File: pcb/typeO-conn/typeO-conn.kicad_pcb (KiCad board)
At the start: 2 copper layers, 24 x 19.6 mm, 9 parts, among them J1 USB_C_Receptacle_USB2.0, J2 Conn_01x05_Male, SW1 SW_DIP_x01

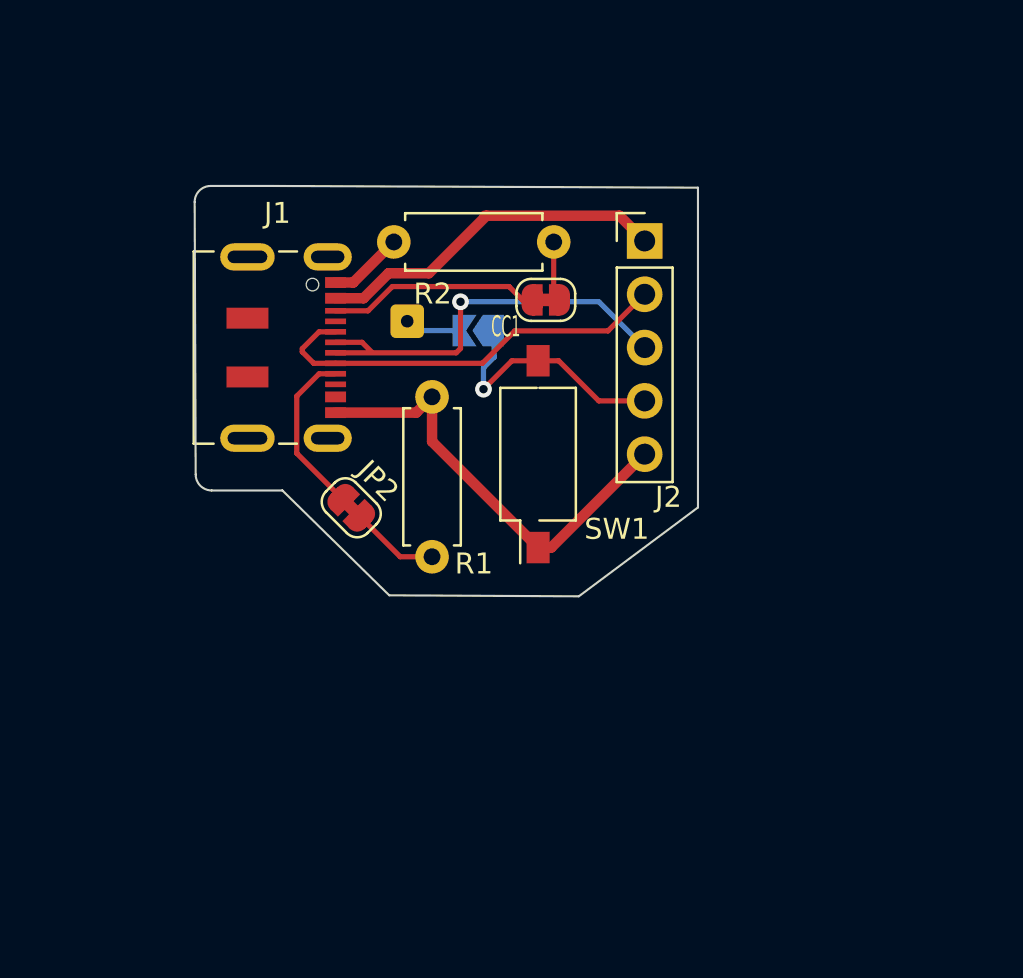
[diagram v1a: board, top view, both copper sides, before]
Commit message: Start work on typeO-conn v2
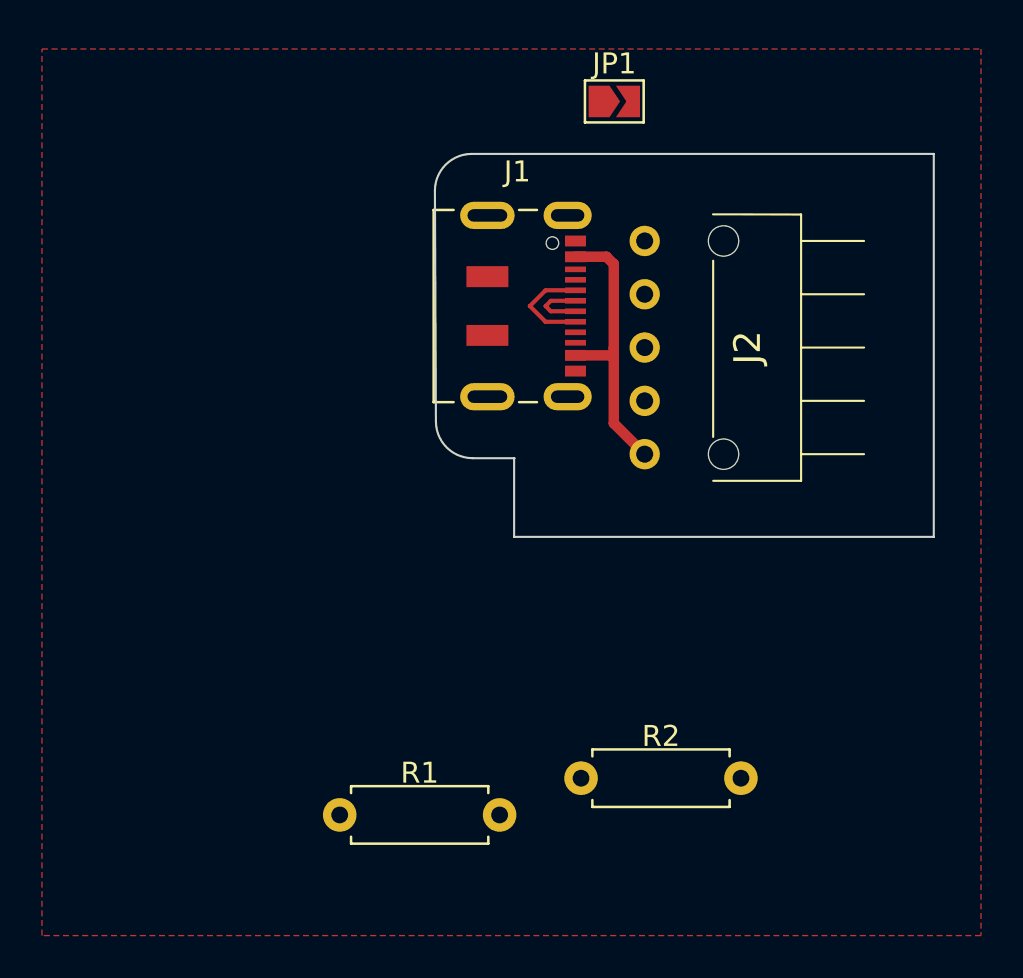
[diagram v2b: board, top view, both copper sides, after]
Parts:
- removed H1: ID, Connector_Wire:SolderWire-0.1sqmm_1x01_D0.4mm_OD1mm
- removed JP2: CC2, Jumper:SolderJumper-2_P1.3mm_Bridged_RoundedPad1.0x1.5mm
- removed JP3: CC1, Jumper:SolderJumper-2_P1.3mm_Bridged_RoundedPad1.0x1.5mm
- removed SW1: SW_DIP_x01, Button_Switch_SMD:SW_DIP_SPSTx01_Slide_Omron_A6S-110x_W8.9mm_P2.54mm
- J2: value Conn_01x05_Male -> 829-22-005-20-001101; footprint Connector_PinHeader_2.54mm:PinHeader_1x05_P2.54mm_Vertical -> MyLibrary:8292200520001101
- JP1: value SolderJumper_2_Open -> SolderJumper_2_Bridged; moved to F.Cu
- moved R2 27.1 mm to (121.4, 101.8)
- moved R1 20.4 mm to (109.9, 103.6), turned to 0 degrees
- moved JP1 12.7 mm to (123.0, 69.6), turned to 0 degrees
- moved J1 11.6 mm to (118.1, 79.3)
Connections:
- net Net-(J1-PadA6) renamed /D+
- J1 pad A1: Net-(J1-PadA1) -> /GND
- J1 pad A12: Net-(J1-PadA1) -> /GND
- J1 pad A4: Net-(J1-PadA4) -> /VBUS
- J1 pad A7: Net-(J1-PadA7) -> /D-
- J1 pad A9: Net-(J1-PadA4) -> /VBUS
- J1 pad B1: Net-(J1-PadA1) -> /GND
- J1 pad B12: Net-(J1-PadA1) -> /GND
- J1 pad B4: Net-(J1-PadA4) -> /VBUS
- J1 pad B7: Net-(J1-PadA7) -> /D-
- J1 pad B9: Net-(J1-PadA4) -> /VBUS
- J2 pad 1: Net-(J1-PadA4) -> /GND
- J2 pad 2: Net-(J1-PadA7) -> /ID
- J2 pad 4: Net-(J2-Pad4) -> /D-
- J2 pad 5: Net-(J1-PadA1) -> /VBUS
- JP1 pad 1: Net-(H1-Pad1) -> /GND
- JP1 pad 2: Net-(J2-Pad4) -> /ID
- R1 pad 1: Net-(J1-PadA1) -> /GND
- R1 pad 2: Net-(R1-Pad2) -> Net-(J1-PadB5)
- R2 pad 1: Net-(J1-PadA1) -> /GND
- R2 pad 2: Net-(R2-Pad2) -> Net-(J1-PadA5)
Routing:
- net Net-(J1-PadA1): track 24.7 -> 0.00 mm
- net Net-(J1-PadA7): track 20.0 -> 0.00 mm
- net Net-(J1-PadA4): track 16.9 -> 0.00 mm
- net /D+: track 19.8 -> 3.06 mm, vias 1 -> 0
- net /VBUS: track 0.00 -> 13.5 mm
- net Net-(J2-Pad4): track 12.1 -> 0.00 mm, vias 1 -> 0
- net Net-(J1-PadA5): track 10.1 -> 0.00 mm
- net Net-(J1-PadB5): track 8.04 -> 0.00 mm
- net /D-: track 0.00 -> 4.97 mm
- net Net-(R1-Pad2): track 4.17 -> 0.00 mm
- net Net-(R2-Pad2): track 2.87 -> 0.00 mm
- net Net-(H1-Pad1): track 2.84 -> 0.00 mm
- added copper zone on F.Cu, net /GND
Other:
- board size 24 x 19.6 mm -> 23.8 x 18.2 mm

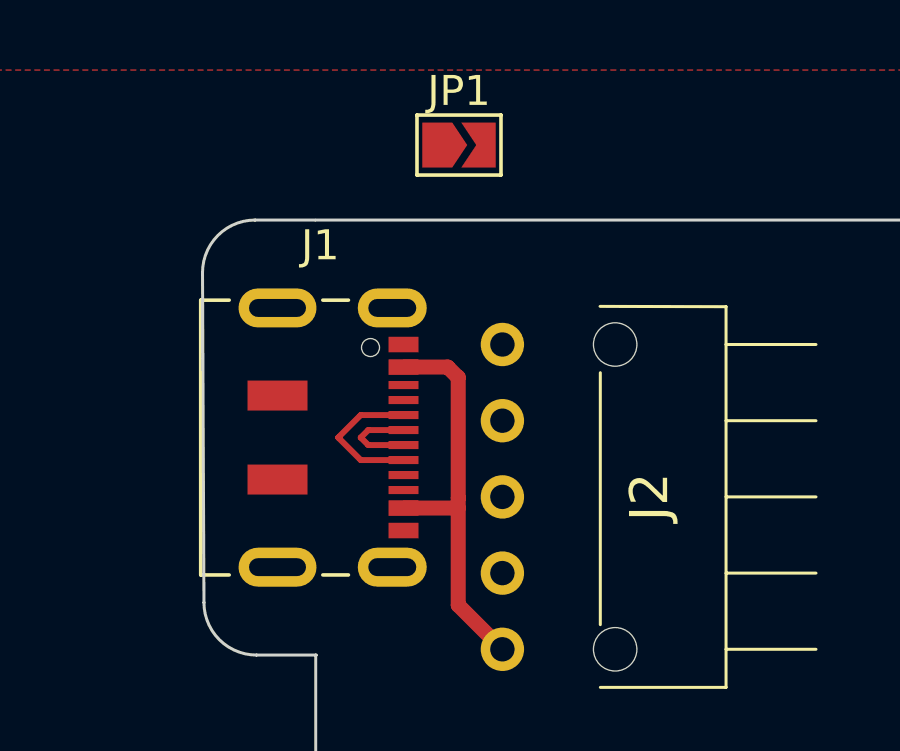
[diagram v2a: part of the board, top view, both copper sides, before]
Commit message: Change resistor values
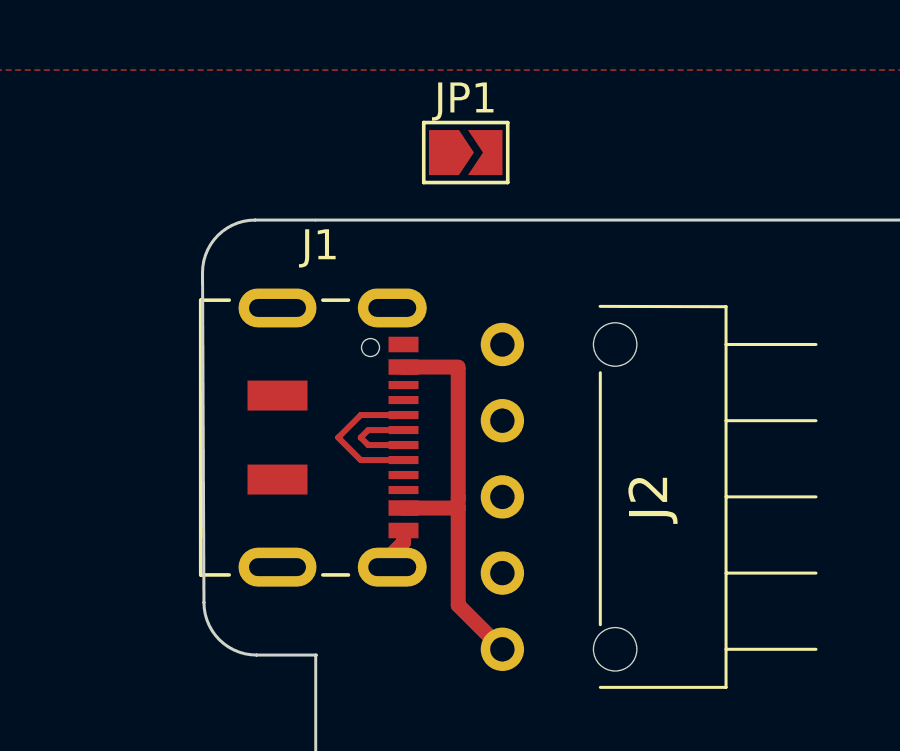
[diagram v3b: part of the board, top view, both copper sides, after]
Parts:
- R1, R2: value 10K -> 5.1k
- moved JP1 0.34 mm to (123.2, 69.8)
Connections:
- J1 pad S1: unconnected-(J1-PadS1) -> /GND
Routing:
- net /GND: track 0.00 -> 1.38 mm
